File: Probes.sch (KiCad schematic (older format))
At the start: 14 parts, among them U3 INA333

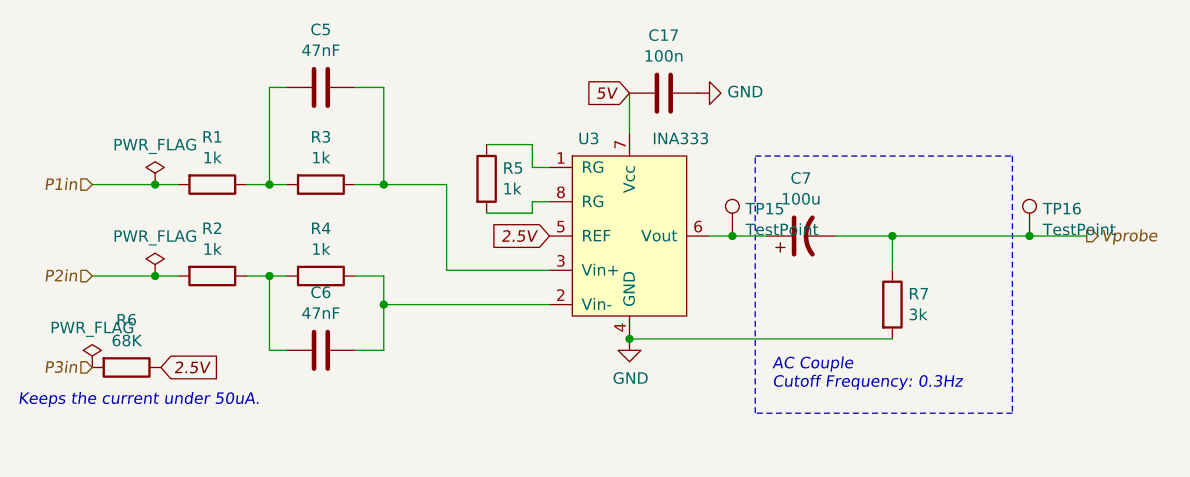
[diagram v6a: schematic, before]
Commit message: #4 - Initial component placement complete. Increased board size.
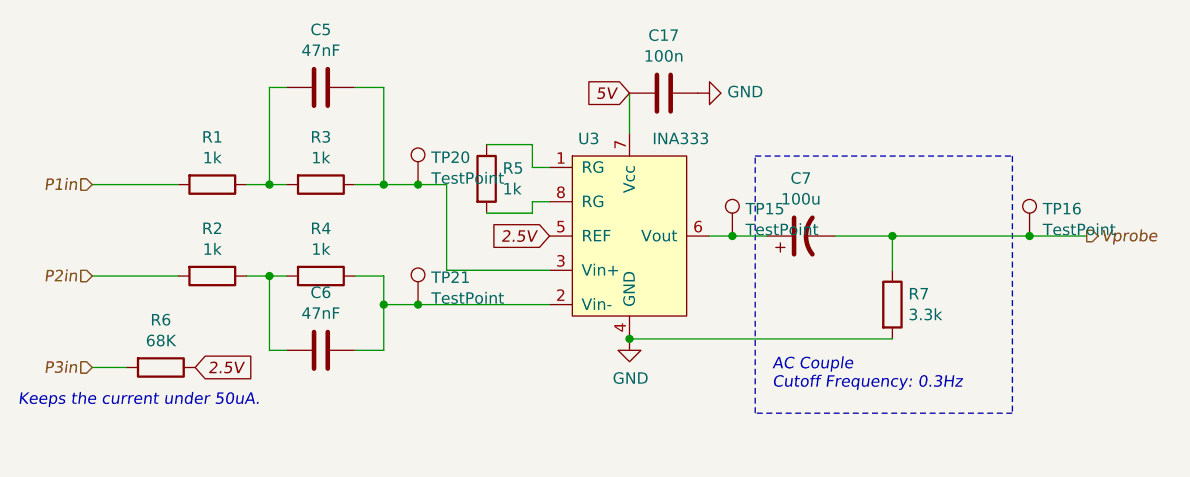
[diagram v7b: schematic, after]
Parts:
- added TP20, TP21: TestPoint, TestPoint:TestPoint_Pad_D2.0mm, symbol Connector:TestPoint
- R7: value 3k -> 3.3k
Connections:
- net at C6.1, R4.1, U3.2 (Vin-): now also TP21.1
- net at C5.1, R3.1, U3.3 (Vin+): now also TP20.1
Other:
- moved on the sheet: R6
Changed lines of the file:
@@
 $EndComp
-Wire Wire Line
-	3750 3325 4025 3325
-Wire Wire Line
-	3750 3725 4025 3725
 Wire Wire Line
 	4425 3325 4525 3325
@@
 	5675 3450 5475 3450
 Wire Wire Line
-	5025 3325 5300 3325
+	5025 3325 5175 3325
 Wire Wire Line
 	5300 3325 5300 3700
@@
 	5300 3700 5750 3700
 Connection ~ 5025 3325
-Wire Wire Line
-	5025 3850 5750 3850
 Connection ~ 5025 3850
 Wire Wire Line
@@
 L Device:R R6
 U 1 1 5FA0AABB
-P 3900 4125
-F 0 "R6" V 3693 4125 50  0000 C CNN
-F 1 "68K" V 3784 4125 50  0000 C CNN
-F 2 "Resistor_SMD:R_0805_2012Metric_Pad1.20x1.40mm_HandSolder" V 3830 4125 50  0001 C CNN
-F 3 "~" H 3900 4125 50  0001 C CNN
-	1    3900 4125
+P 4050 4125
+F 0 "R6" V 3843 4125 50  0000 C CNN
+F 1 "68K" V 3934 4125 50  0000 C CNN
+F 2 "Resistor_SMD:R_0805_2012Metric_Pad1.20x1.40mm_HandSolder" V 3980 4125 50  0001 C CNN
+F 3 "~" H 4050 4125 50  0001 C CNN
+	1    4050 4125
 	0    1    1    0
 $EndComp
-Text GLabel 4050 4125 2    50   Input Italic 0
+Text GLabel 4200 4125 2    50   Input Italic 0
 2.5V
 Text Notes 3425 4300 0    50   Italic 0
@@
 P 7250 3850
 F 0 "R7" H 7320 3896 50  0000 L CNN
-F 1 "3k" H 7320 3805 50  0000 L CNN
+F 1 "3.3k" H 7320 3805 50  0000 L CNN
 F 2 "Resistor_SMD:R_0805_2012Metric_Pad1.20x1.40mm_HandSolder" V 7180 3850 50  0001 C CNN
 F 3 "~" H 7250 3850 50  0001 C CNN
@@
 Text HLabel 8100 3550 2    50   Output Italic 0
 Vprobe
-Text HLabel 3750 3325 0    50   Input Italic 0
-P1in
 Text HLabel 3750 3725 0    50   Input Italic 0
 P2in
 Text HLabel 3750 4125 0    50   Input Italic 0
 P3in
-$Comp
-L power:PWR_FLAG #FLG0105
-U 1 1 5FBE4DBA
-P 4025 3325
-F 0 "#FLG0105" H 4025 3400 50  0001 C CNN
-F 1 "PWR_FLAG" H 4025 3498 50  0000 C CNN
-F 2 "" H 4025 3325 50  0001 C CNN
-F 3 "~" H 4025 3325 50  0001 C CNN
-	1    4025 3325
-	1    0    0    -1
-$EndComp
-Connection ~ 4025 3325
-Wire Wire Line
-	4025 3325 4125 3325
-$Comp
-L power:PWR_FLAG #FLG0106
-U 1 1 5FBE57AC
-P 4025 3725
-F 0 "#FLG0106" H 4025 3800 50  0001 C CNN
-F 1 "PWR_FLAG" H 4025 3898 50  0000 C CNN
-F 2 "" H 4025 3725 50  0001 C CNN
-F 3 "~" H 4025 3725 50  0001 C CNN
-	1    4025 3725
-	1    0    0    -1
-$EndComp
-Connection ~ 4025 3725
-Wire Wire Line
-	4025 3725 4125 3725
-$Comp
-L power:PWR_FLAG #FLG0107
-U 1 1 5FBE5B53
-P 3750 4125
-F 0 "#FLG0107" H 3750 4200 50  0001 C CNN
-F 1 "PWR_FLAG" H 3750 4298 50  0000 C CNN
-F 2 "" H 3750 4125 50  0001 C CNN
-F 3 "~" H 3750 4125 50  0001 C CNN
-	1    3750 4125
-	1    0    0    -1
-$EndComp
 $Comp
 L Connector:TestPoint TP15
@@
 	6100 2925 6100 3100
 Connection ~ 6100 4000
+Wire Wire Line
+	3750 4125 3900 4125
+Text HLabel 3750 3325 0    50   Input Italic 0
+P1in
+$Comp
+L Connector:TestPoint TP20
+U 1 1 5FD43418
+P 5175 3325
+F 0 "TP20" H 5233 3443 50  0000 L CNN
+F 1 "TestPoint" H 5233 3352 50  0000 L CNN
+F 2 "TestPoint:TestPoint_Pad_D2.0mm" H 5375 3325 50  0001 C CNN
+F 3 "~" H 5375 3325 50  0001 C CNN
+	1    5175 3325
+	1    0    0    -1
+$EndComp
+$Comp
+L Connector:TestPoint TP21
+U 1 1 5FD43A26
+P 5175 3850
+F 0 "TP21" H 5233 3968 50  0000 L CNN
+F 1 "TestPoint" H 5233 3877 50  0000 L CNN
+F 2 "TestPoint:TestPoint_Pad_D2.0mm" H 5375 3850 50  0001 C CNN
+F 3 "~" H 5375 3850 50  0001 C CNN
+	1    5175 3850
+	1    0    0    -1
+$EndComp
+Connection ~ 5175 3325
+Wire Wire Line
+	5175 3325 5300 3325
+Connection ~ 5175 3850
+Wire Wire Line
+	5175 3850 5750 3850
+Wire Wire Line
+	5025 3850 5175 3850
+Wire Wire Line
+	3750 3325 4125 3325
+Wire Wire Line
+	3750 3725 4125 3725
 $EndSCHEMATC

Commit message: #5 - Added 3.3V buck-boost regulator
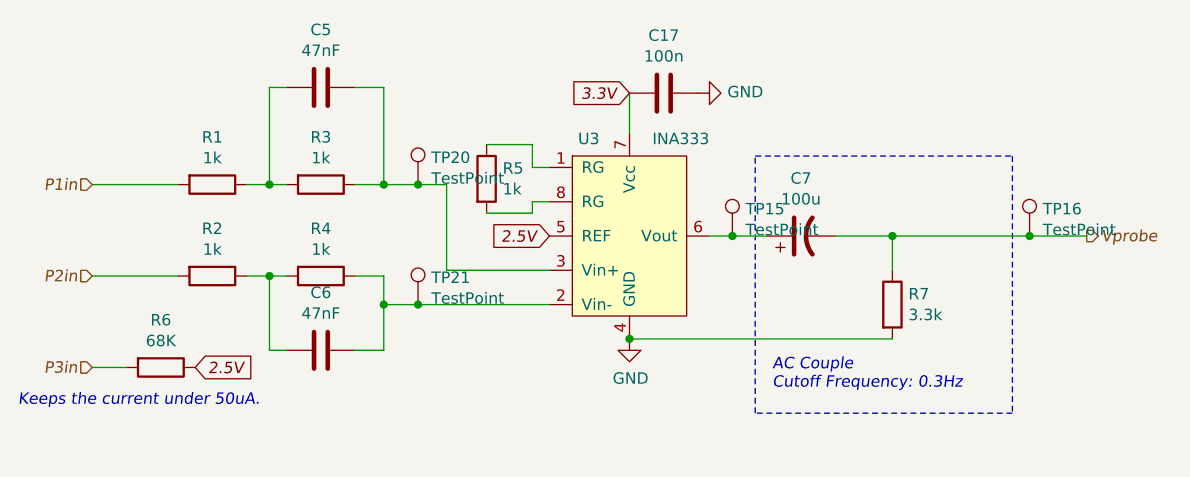
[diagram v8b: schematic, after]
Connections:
- net 5V renamed 3.3V
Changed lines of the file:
@@
 $EndComp
 Text GLabel 6100 2925 0    50   Input Italic 0
-5V
+3.3V
 $Comp
 L Device:R R6
